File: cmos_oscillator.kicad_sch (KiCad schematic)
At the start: 5 parts, among them X1 YC24.576MUBCE2O

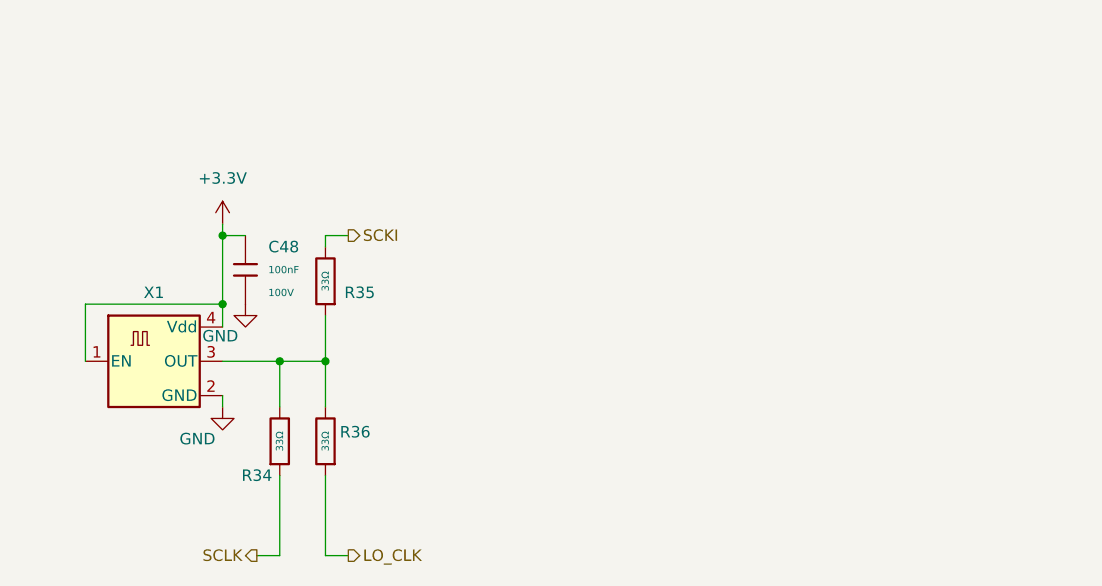
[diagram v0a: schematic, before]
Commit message: Fixed DAC
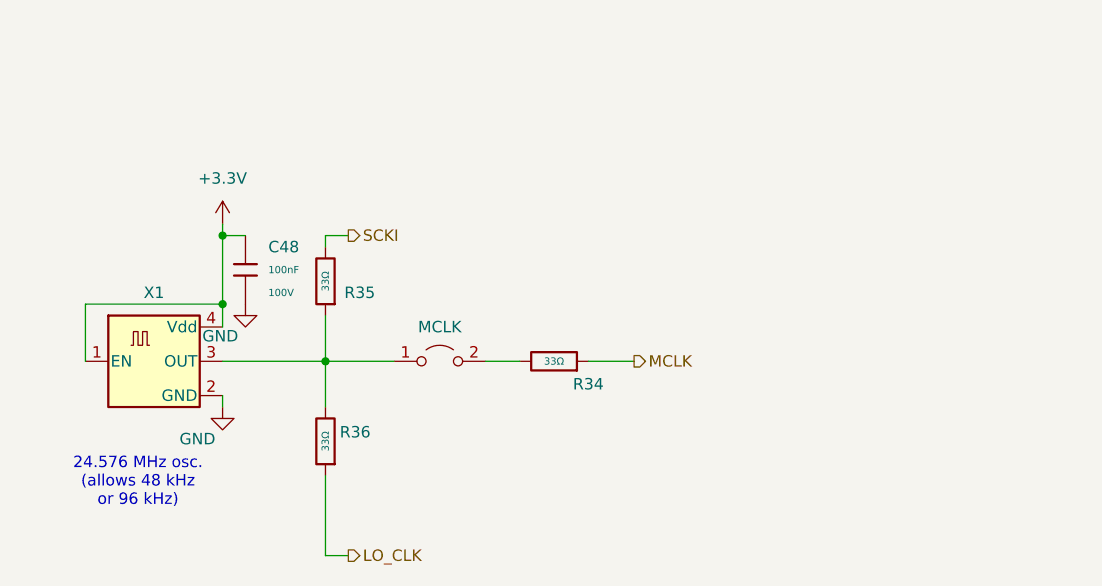
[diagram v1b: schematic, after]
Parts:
- added JP5: MCLK, Jumper:SolderJumper-2_P1.3mm_Open_RoundedPad1.0x1.5mm, symbol Jumper:Jumper_2_Open
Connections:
- net at R35.1, R36.2, X1.3 (OUT): now also JP5.1 (A); no longer R34.2
- net SCLK renamed MCLK
- new net: JP5.2 (B), R34.2
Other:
- note added: "24.576 MHz osc. (allows 48 kHz or 96 kHz)"
- moved on the sheet: R34
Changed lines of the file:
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@@
 	(generator_version "9.0")
 	(paper "A")
+	(text "24.576 MHz osc.\n(allows 48 kHz \nor 96 kHz)"
+		(exclude_from_sim no)
+		(at 139.192 112.522 0)
+		(effects
+			(font
+				(size 1.27 1.27)
+			)
+		)
+	)
 	(junction
 		(at 160.02 99.06)
@@
 		(color 0 0 0 0)
 	)
-	(junction
-		(at 154.94 99.06)
-		(diameter 0)
-		(color 0 0 0 0)
-	)
 	(wire
 		(pts
@@
 	(wire
 		(pts
+			(xy 160.02 99.06) (xy 167.64 99.06)
+		)
+		(stroke
+			(width 0)
+			(type default)
+		)
+	)
+	(wire
+		(pts
 			(xy 160.02 120.65) (xy 160.02 111.76)
 		)
@@
 	(wire
 		(pts
-			(xy 148.59 99.06) (xy 154.94 99.06)
-		)
-		(stroke
-			(width 0)
-			(type default)
-		)
-	)
-	(wire
-		(pts
 			(xy 148.59 102.87) (xy 148.59 104.14)
 		)
@@
 	(wire
 		(pts
-			(xy 154.94 120.65) (xy 154.94 111.76)
-		)
-		(stroke
-			(width 0)
-			(type default)
-		)
-	)
-	(wire
-		(pts
-			(xy 154.94 99.06) (xy 160.02 99.06)
+			(xy 177.8 99.06) (xy 181.61 99.06)
+		)
+		(stroke
+			(width 0)
+			(type default)
+		)
+	)
+	(wire
+		(pts
+			(xy 148.59 99.06) (xy 160.02 99.06)
 		)
 		(stroke
@@
 	(wire
 		(pts
-			(xy 152.4 120.65) (xy 154.94 120.65)
+			(xy 189.23 99.06) (xy 194.31 99.06)
 		)
 		(stroke
@@
 		(pts
 			(xy 162.56 85.09) (xy 160.02 85.09)
-		)
-		(stroke
-			(width 0)
-			(type default)
-		)
-	)
-	(wire
-		(pts
-			(xy 154.94 99.06) (xy 154.94 104.14)
 		)
 		(stroke
@@
 		)
 	)
-	(hierarchical_label "SCLK"
+	(hierarchical_label "MCLK"
 		(shape output)
-		(at 152.4 120.65 180)
+		(at 194.31 99.06 0)
 		(effects
 			(font
 				(size 1.27 1.27)
 			)
-			(justify right)
+			(justify left)
 		)
 	)
@@
 	)
 	(symbol
+		(lib_id "Jumper:Jumper_2_Open")
+		(at 172.72 99.06 0)
+		(unit 1)
+		(exclude_from_sim no)
+		(in_bom yes)
+		(on_board yes)
+		(dnp no)
+		(fields_autoplaced yes)
+		(property "Reference" "JP5"
+			(at 172.72 92.71 0)
+			(effects
+				(font
+					(size 1.27 1.27)
+				)
+				(hide yes)
+			)
+		)
+		(property "Value" "MCLK"
+			(at 172.72 95.25 0)
+			(effects
+				(font
+					(size 1.27 1.27)
+				)
+			)
+		)
+		(property "Footprint" "Jumper:SolderJumper-2_P1.3mm_Open_RoundedPad1.0x1.5mm"
+			(at 172.72 99.06 0)
+			(effects
+				(font
+					(size 1.27 1.27)
+				)
+				(hide yes)
+			)
+		)
+		(property "Datasheet" "~"
+			(at 172.72 99.06 0)
+			(effects
+				(font
+					(size 1.27 1.27)
+				)
+				(hide yes)
+			)
+		)
+		(property "Description" ""
+			(at 172.72 99.06 0)
+			(effects
+				(font
+					(size 1.27 1.27)
+				)
+				(hide yes)
+			)
+		)
+		(property "JLCPCB #" ""
+			(at 172.72 99.06 0)
+			(effects
+				(font
+					(size 1.27 1.27)
+				)
+				(hide yes)
+			)
+		)
+		(pin "1"
+		)
+		(pin "2"
+		)
+		(instances
+			(project "Intro-to-CAD-2026"
+				(path "/c12dc015-e6cb-468c-8de4-269c3106de0e/1bf8039c-3ec8-4592-8d3c-78300c63b601"
+					(reference "JP5")
+					(unit 1)
+				)
+			)
+		)
+	)
+	(symbol
 		(lib_id "power:GND")
 		(at 148.59 104.14 0)
@@
 	(symbol
 		(lib_id "PCM_JLCPCB-Resistors:0805,33Ω")
-		(at 154.94 107.95 0)
+		(at 185.42 99.06 270)
 		(mirror x)
 		(unit 1)
@@
 		(dnp no)
 		(property "Reference" "R34"
-			(at 152.4 111.76 0)
+			(at 189.23 101.6 90)
 			(effects
 				(font
@@
 		)
 		(property "Value" "33Ω"
-			(at 154.94 107.95 90)
+			(at 185.42 99.06 90)
 			(do_not_autoplace yes)
 			(effects
@@
 		)
 		(property "Footprint" "PCM_JLCPCB:R_0805"
-			(at 153.162 107.95 90)
+			(at 185.42 100.838 90)
 			(effects
 				(font
@@
 		)
 		(property "Datasheet" "https://www.lcsc.com/datasheet/lcsc_datasheet_2205311830_UNI-ROYAL-Uniroyal-Elec-0805W8F330JT5E_C17634.pdf"
-			(at 154.94 107.95 0)
+			(at 185.42 99.06 0)
 			(effects
 				(font
@@
 		)
 		(property "Description" "125mW Thick Film Resistors 150V ±1% ±200ppm/°C 33Ω 0805 Chip Resistor - Surface Mount ROHS"
-			(at 154.94 107.95 0)
+			(at 185.42 99.06 0)
 			(effects
 				(font
@@
 		)
 		(property "LCSC" "C17634"
-			(at 154.94 107.95 0)
+			(at 185.42 99.06 0)
 			(effects
 				(font
@@
 		)
 		(property "Stock" "335994"
-			(at 154.94 107.95 0)
+			(at 185.42 99.06 0)
 			(effects
 				(font
@@
 		)
 		(property "Price" "0.005USD"
-			(at 154.94 107.95 0)
+			(at 185.42 99.06 0)
 			(effects
 				(font
@@
 		)
 		(property "Process" "SMT"
-			(at 154.94 107.95 0)
+			(at 185.42 99.06 0)
 			(effects
 				(font
@@
 		)
 		(property "Minimum Qty" "20"
-			(at 154.94 107.95 0)
+			(at 185.42 99.06 0)
 			(effects
 				(font
@@
 		)
 		(property "Attrition Qty" "10"
-			(at 154.94 107.95 0)
+			(at 185.42 99.06 0)
 			(effects
 				(font
@@
 		)
 		(property "Class" "Basic Component"
-			(at 154.94 107.95 0)
+			(at 185.42 99.06 0)
 			(effects
 				(font
@@
 		)
 		(property "Category" "Resistors,Chip Resistor - Surface Mount"
-			(at 154.94 107.95 0)
+			(at 185.42 99.06 0)
 			(effects
 				(font
@@
 		)
 		(property "Manufacturer" "UNI-ROYAL(Uniroyal Elec)"
-			(at 154.94 107.95 0)
+			(at 185.42 99.06 0)
 			(effects
 				(font
@@
 		)
 		(property "Part" "0805W8F330JT5E"
-			(at 154.94 107.95 0)
+			(at 185.42 99.06 0)
 			(effects
 				(font
@@
 		)
 		(property "Resistance" "33Ω"
-			(at 154.94 107.95 0)
+			(at 185.42 99.06 0)
 			(effects
 				(font
@@
 		)
 		(property "Power(Watts)" "125mW"
-			(at 154.94 107.95 0)
+			(at 185.42 99.06 0)
 			(effects
 				(font
@@
 		)
 		(property "Type" "Thick Film Resistors"
-			(at 154.94 107.95 0)
+			(at 185.42 99.06 0)
 			(effects
 				(font
@@
 		)
 		(property "Overload Voltage (Max)" "150V"
-			(at 154.94 107.95 0)
+			(at 185.42 99.06 0)
 			(effects
 				(font
@@
 		)
 		(property "Operating Temperature Range" "-55°C~+155°C"
-			(at 154.94 107.95 0)
+			(at 185.42 99.06 0)
 			(effects
 				(font
@@
 		)
 		(property "Tolerance" "±1%"
-			(at 154.94 107.95 0)
+			(at 185.42 99.06 0)
 			(effects
 				(font
@@
 		)
 		(property "Temperature Coefficient" "±200ppm/°C"
-			(at 154.94 107.95 0)
+			(at 185.42 99.06 0)
 			(effects
 				(font
@@
 		)
 		(instances
-			(project "Frohne"
+			(project "Intro-to-CAD-2026"
 				(path "/c12dc015-e6cb-468c-8de4-269c3106de0e/1bf8039c-3ec8-4592-8d3c-78300c63b601"
 					(reference "R34")

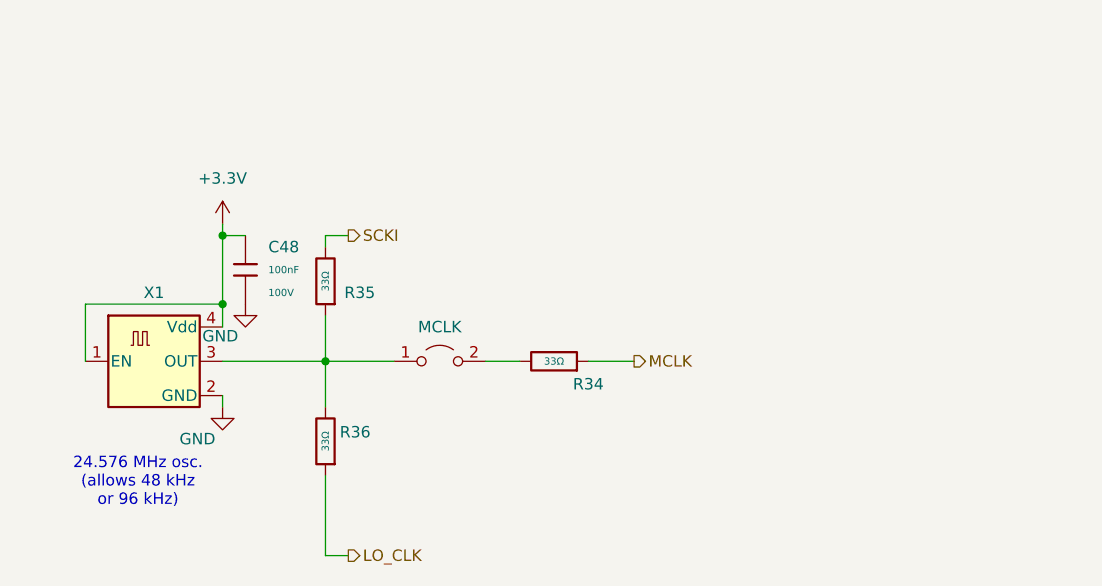
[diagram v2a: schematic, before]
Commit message: Adding fixes:
LDO for LO.  Reduce gain by 10/1.5.  Add better bypassing for VDDA/2 and CMOS Oscillator.  Added Johnson counter.  This is schematic only at the moment.
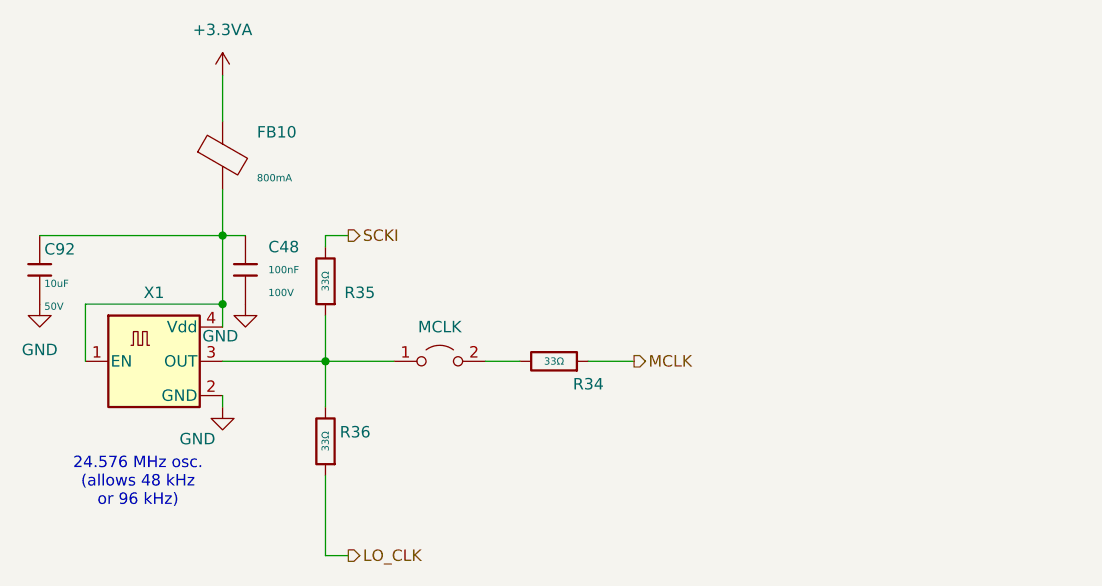
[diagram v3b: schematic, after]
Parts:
- added C92: 10uF, PCM_JLCPCB:C_1206, symbol PCM_JLCPCB-Capacitors:1206,10uF
- added FB10: (no value), PCM_JLCPCB:FB_0805, symbol PCM_JLCPCB-Inductors:Ferrite,0805
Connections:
- net GND: now also C92.2
- net +3.3V: no longer names the net of C48.1, X1.1 (EN), X1.4 (Vdd)
- net +3.3V: now also C92.1, FB10.2
- new net +3.3VA: FB10.1

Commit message: Added CJC5340
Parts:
- removed JP5: MCLK, Jumper:SolderJumper-2_P1.3mm_Open_RoundedPad1.0x1.5mm, symbol Jumper:Jumper_2_Open
- added R76: 33Ω, PCM_JLCPCB:R_0805, symbol PCM_JLCPCB-Resistors:0805,33Ω
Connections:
- net at R35.1, R36.2, X1.3 (OUT): now also R34.2, R76.2
- net SCKI renamed SCKI1
- new net SCKI2: R76.1
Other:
- moved on the sheet: R35

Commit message: Placed the second ADC
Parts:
- C48, C92: Manufacturer Samsung Electro-Mechanics -> (none)
- FB10: Manufacturer Sunlord -> (none)
- R34, R35, R36, R76: Manufacturer UNI-ROYAL(Uniroyal Elec) -> (none)
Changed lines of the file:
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@@
-			)
-		)
-		(property "Manufacturer" "UNI-ROYAL(Uniroyal Elec)"
-			(at 160.02 83.82 0)
-			(hide yes)
-			(show_name no)
-			(do_not_autoplace no)
-			(effects
-				(font
-					(size 1.27 1.27)
-				)
 			)
 		)
@@
 		)
 		(property "Category" "Filters/EMI Optimization,Ferrite Beads"
-			(at 148.59 76.2 0)
-			(hide yes)
-			(show_name no)
-			(do_not_autoplace no)
-			(effects
-				(font
-					(size 1.27 1.27)
-				)
-			)
-		)
-		(property "Manufacturer" "Sunlord"
 			(at 148.59 76.2 0)
 			(hide yes)
@@
 			)
 		)
-		(property "Manufacturer" "Samsung Electro-Mechanics"
-			(at 128.27 88.9 0)
-			(hide yes)
-			(show_name no)
-			(do_not_autoplace no)
-			(effects
-				(font
-					(size 1.27 1.27)
-				)
-			)
-		)
 		(property "Part" "CL31A106KBHNNNE"
 			(at 128.27 88.9 0)
@@
 		)
 		(property "Category" "Resistors,Chip Resistor - Surface Mount"
-			(at 185.42 91.44 0)
-			(hide yes)
-			(show_name no)
-			(do_not_autoplace no)
-			(effects
-				(font
-					(size 1.27 1.27)
-				)
-			)
-		)
-		(property "Manufacturer" "UNI-ROYAL(Uniroyal Elec)"
 			(at 185.42 91.44 0)
 			(hide yes)
@@
 			)
 		)
-		(property "Manufacturer" "Samsung Electro-Mechanics"
-			(at 151.13 88.9 0)
-			(hide yes)
-			(show_name no)
-			(do_not_autoplace no)
-			(effects
-				(font
-					(size 1.27 1.27)
-				)
-			)
-		)
 		(property "Part" "CL21B104KCFNNNE"
 			(at 151.13 88.9 0)
@@
 		)
 		(property "Category" "Resistors,Chip Resistor - Surface Mount"
-			(at 160.02 107.95 0)
-			(hide yes)
-			(show_name no)
-			(do_not_autoplace no)
-			(effects
-				(font
-					(size 1.27 1.27)
-				)
-			)
-		)
-		(property "Manufacturer" "UNI-ROYAL(Uniroyal Elec)"
 			(at 160.02 107.95 0)
 			(hide yes)
@@
 			(at 185.42 99.06 0)
 			(hide yes)
-			(show_name no)
-			(do_not_autoplace no)
-			(effects
-				(font
-					(size 1.27 1.27)
-				)
-			)
-		)
-		(property "Manufacturer" "UNI-ROYAL(Uniroyal Elec)"
-			(at 185.42 99.06 0)
-			(hide yes)

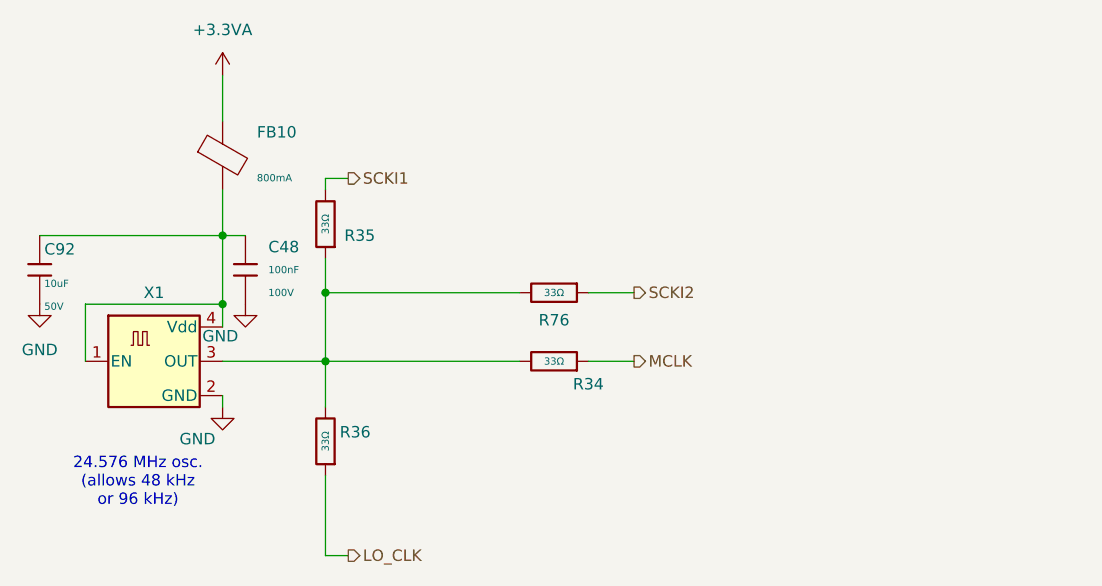
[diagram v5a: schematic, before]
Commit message: Funny thing, SCXI1 and SCKI2 are mixed up, PCB vs Schematic
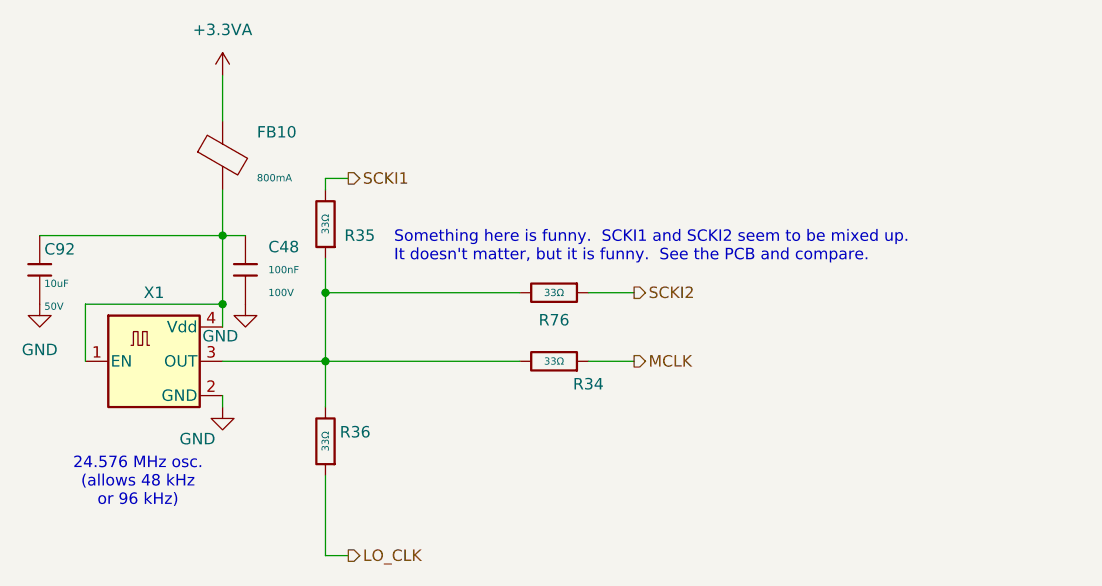
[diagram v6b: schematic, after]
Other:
- note added: "Something here is funny. SCKI1 and SCKI2 seem to be mixed up. It doesn't matter, but it is funny. See the PCB and compare."
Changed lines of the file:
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@@
 	(generator_version "10.0")
 	(paper "A")
+	(text "Something here is funny.  SCKI1 and SCKI2 seem to be mixed up.\nIt doesn't matter, but it is funny.  See the PCB and compare."
+		(exclude_from_sim no)
+		(at 167.64 86.36 0)
+		(effects
+			(font
+				(size 1.27 1.27)
+			)
+			(justify left)
+		)
+	)
 	(text "24.576 MHz osc.\n(allows 48 kHz \nor 96 kHz)"
 		(exclude_from_sim no)
